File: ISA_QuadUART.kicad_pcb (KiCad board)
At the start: 2 copper layers, 104.1 x 102.9 mm, 42 parts, among them J1 ISA BUS, J11 Serial 4 IDC, J12 Serial 3 IDC, J13 UART4_SEL, J2 ADDR_IRQ, J3 UART1_SEL, J4 UART2_SEL, J5 ADDR, J7 Serial 1 DB9, J8 UART3_SEL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

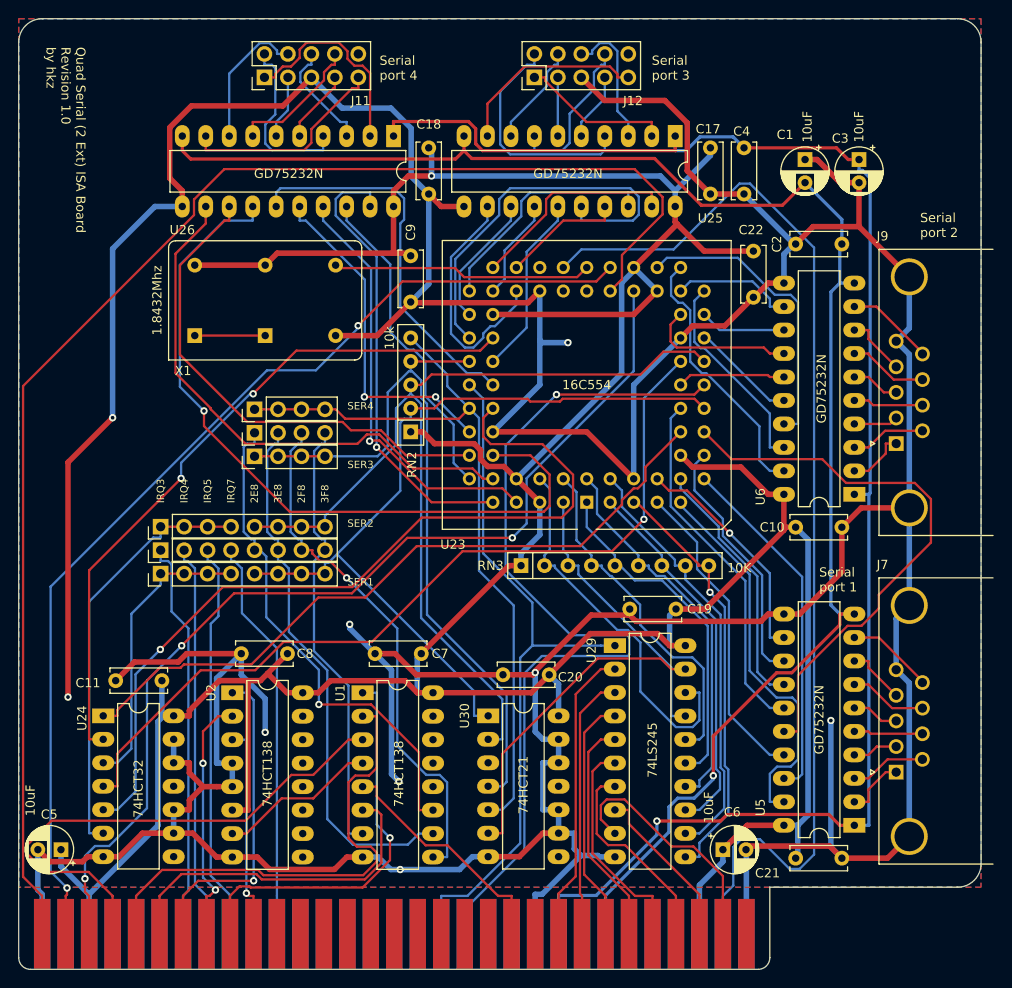
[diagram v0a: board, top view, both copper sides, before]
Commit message: Redone some power traces
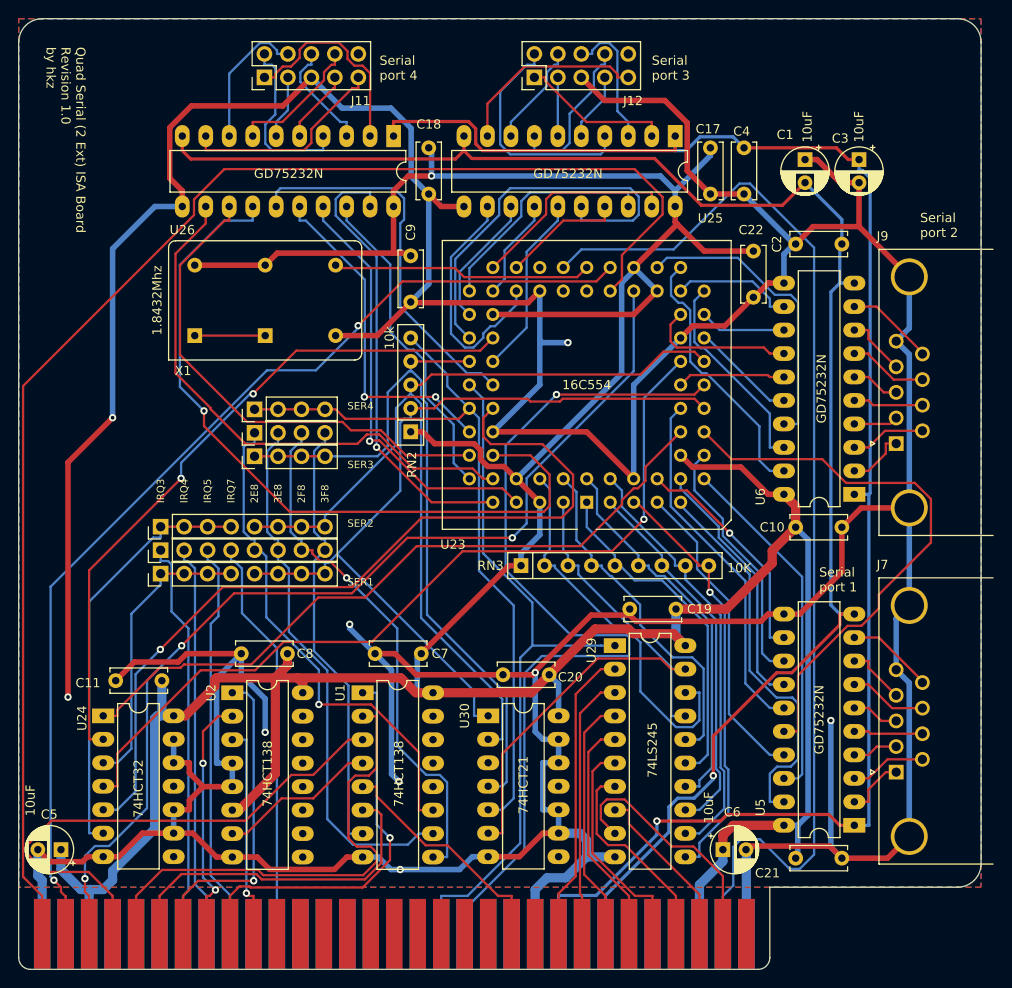
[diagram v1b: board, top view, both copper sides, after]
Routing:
- net VCC: track 408.4 -> 414.0 mm
- net GND: track 652.6 -> 653.5 mm
